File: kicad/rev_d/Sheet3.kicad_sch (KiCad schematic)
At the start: 98 parts, among them U1 74HCT1G04, X10 ST-214C, X14 AAFP/AC97 audio, X16 PLB1-4I, X17 PLB1-4I, X18 PLB1-4I, X20 PLB1-4I

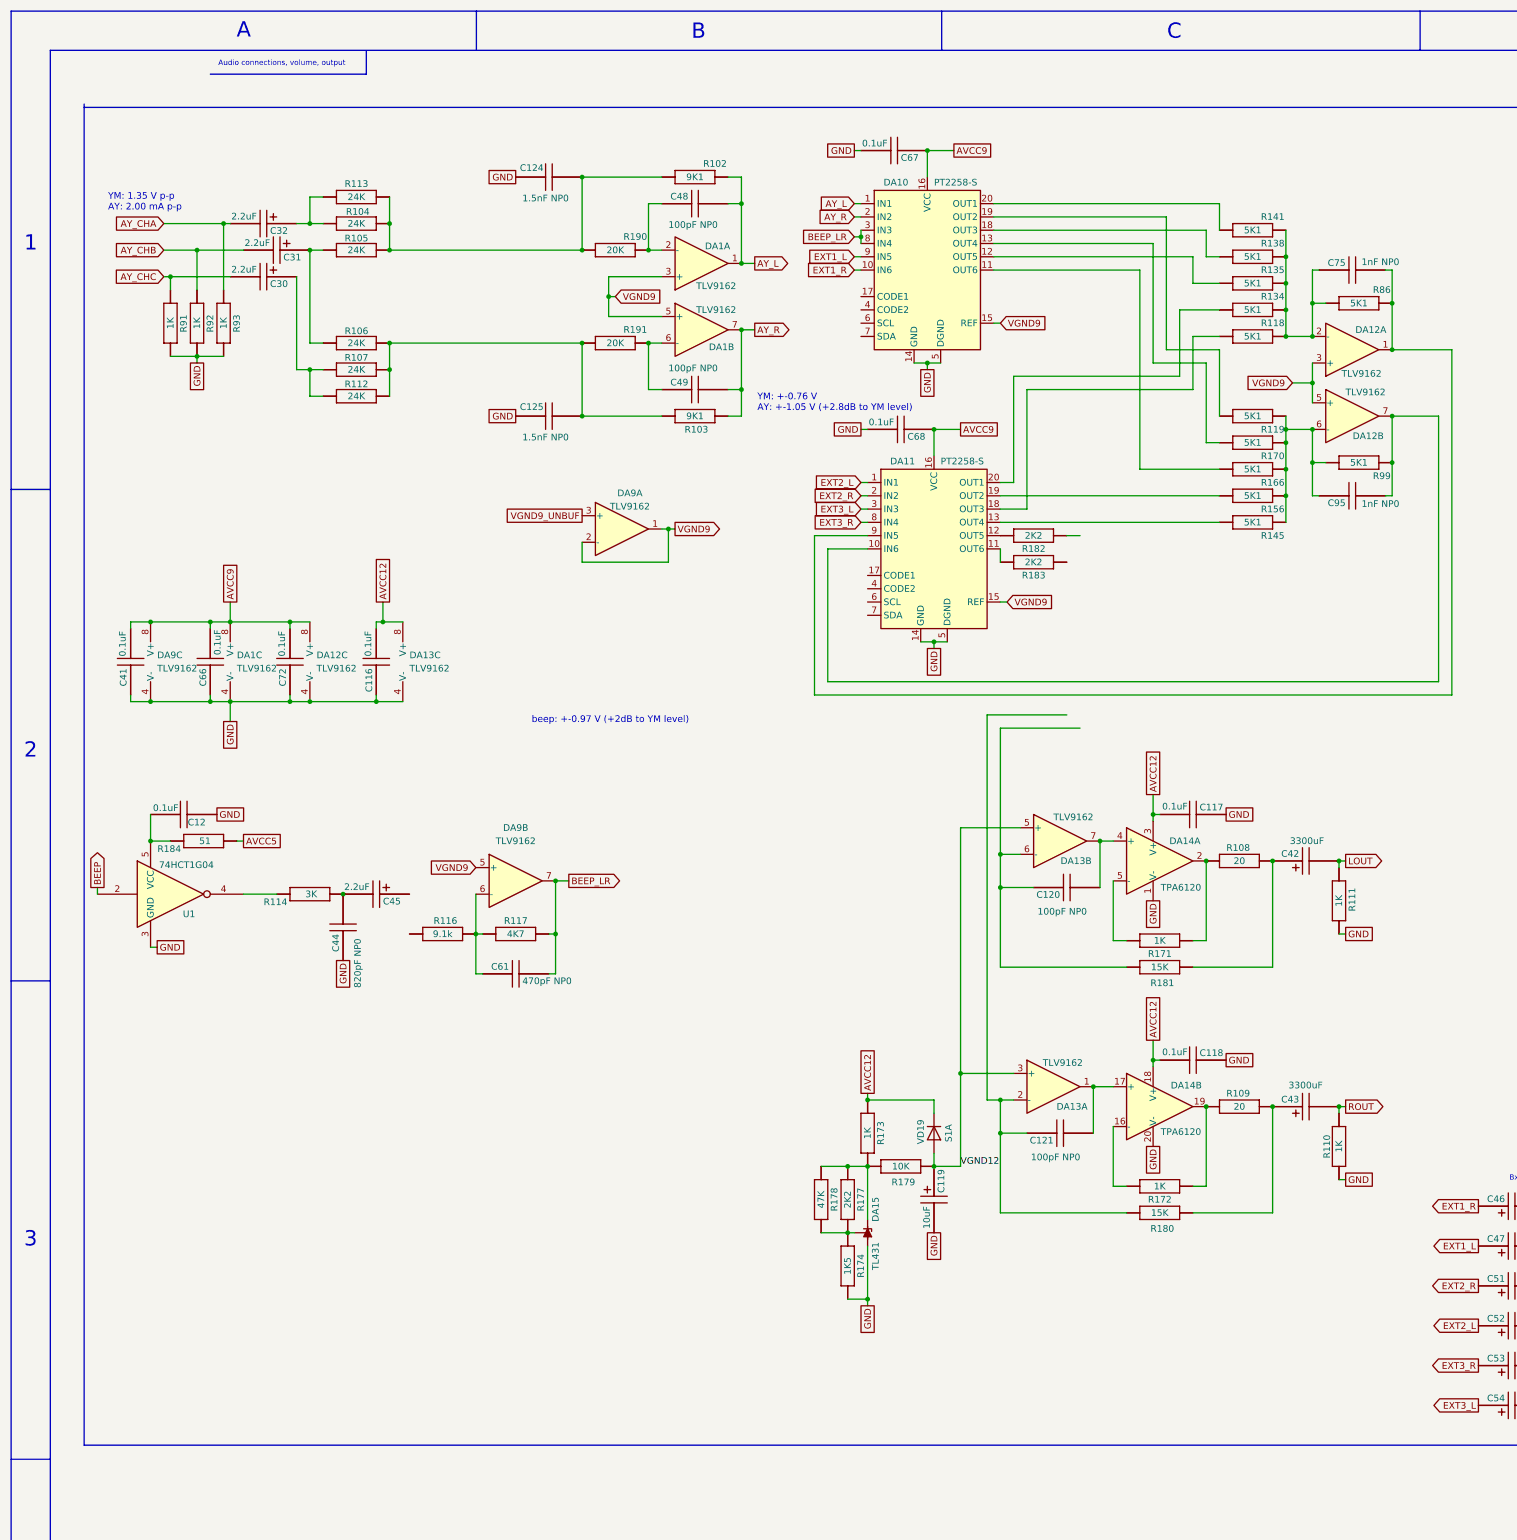
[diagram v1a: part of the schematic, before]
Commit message: pentevo: rev D: changed amplification for YM, added AY -3dB pad, remade lowpass for AY, added some ideas regarding highpass (WIP)
git-svn-id: svn://localhost/local-pentevo@1241 c6c76956-fad2-4150-a3a9-ea0a427205ba
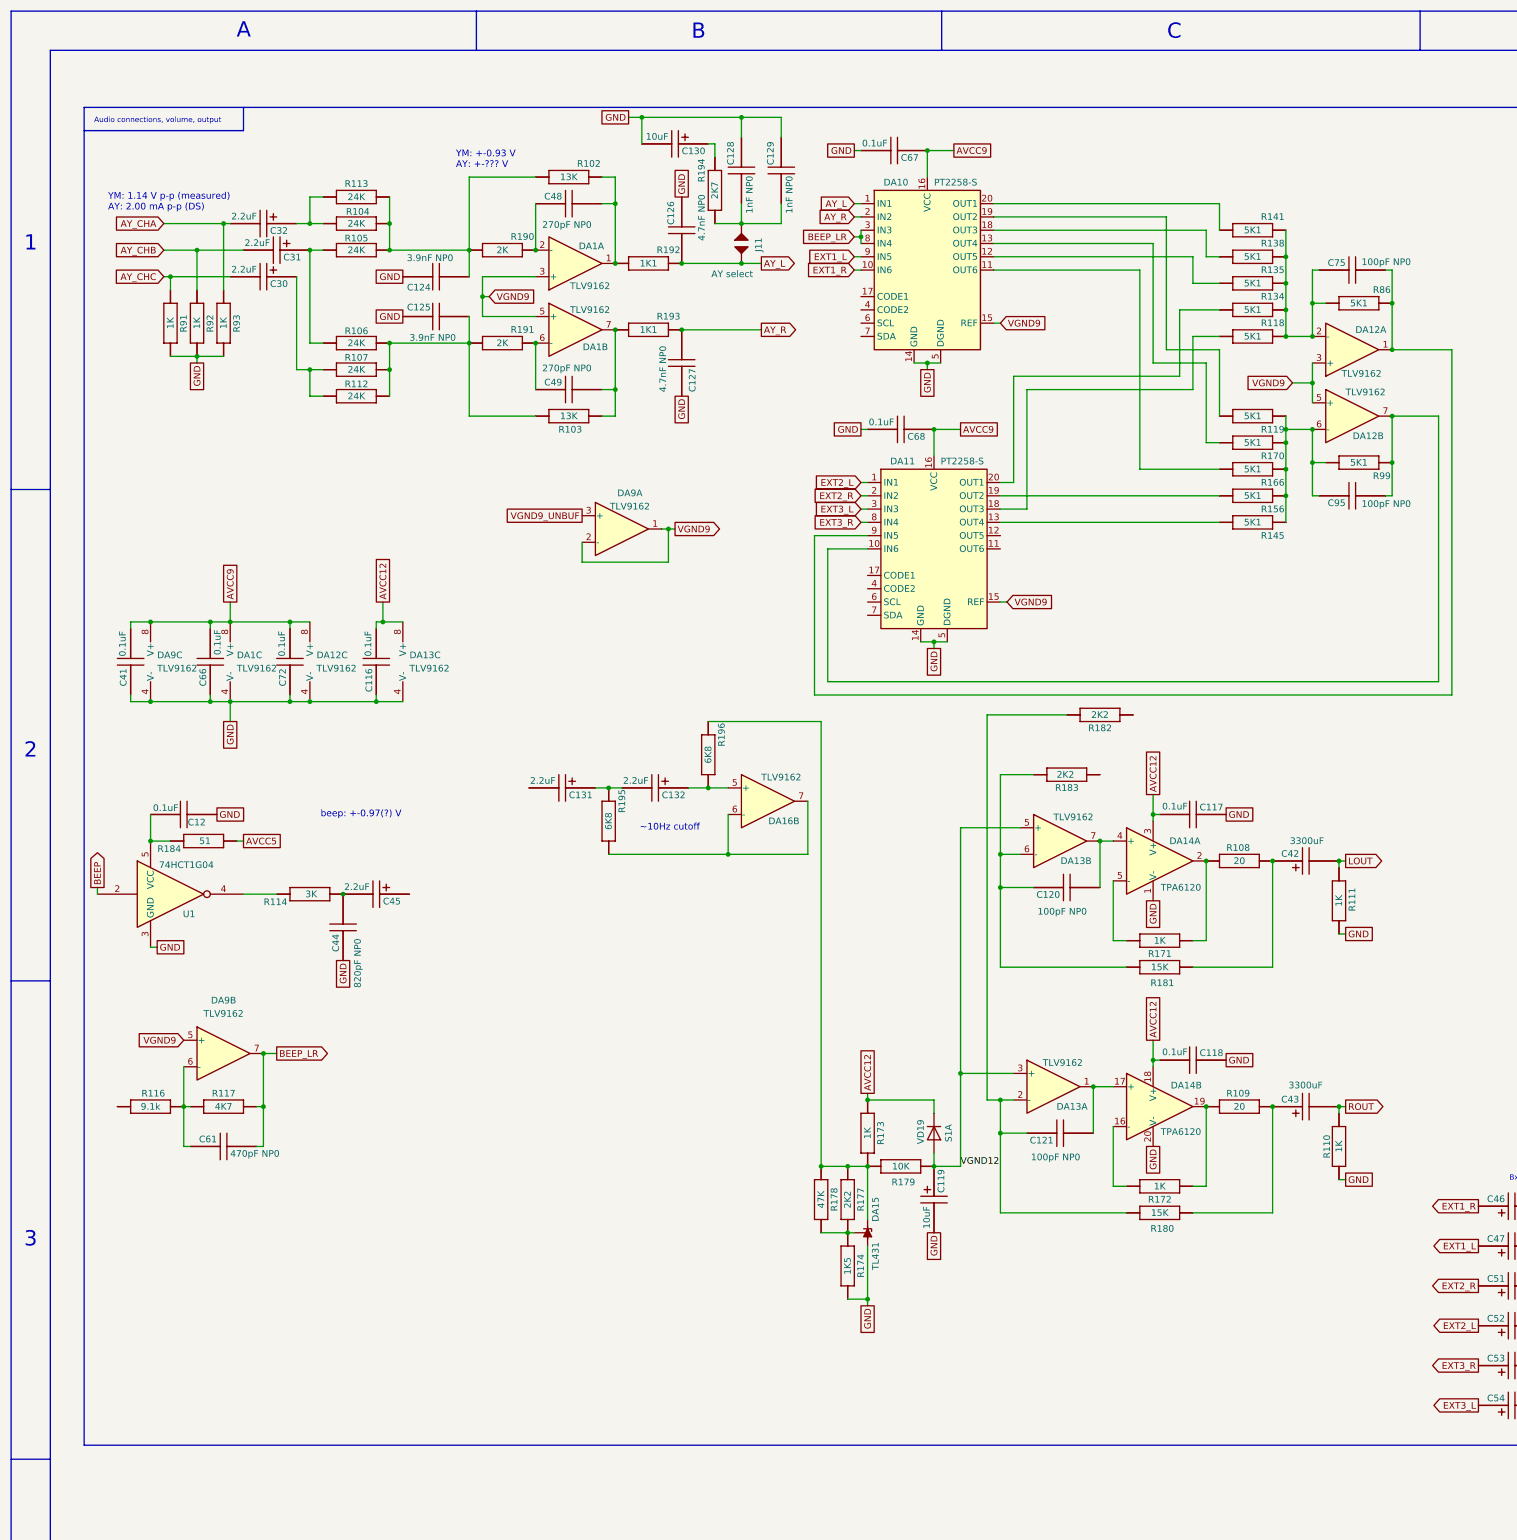
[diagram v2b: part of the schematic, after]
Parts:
- added C126, C127: 4.7nF NP0, C-CHIP, symbol eva-altium-import:Sheet2_0_CAPCHIP
- added C128, C129: 1nF NP0, C-CHIP, symbol eva-altium-import:Sheet2_0_CAPCHIP
- added C130: 10uF, EC-CHIP, symbol eva-altium-import:Sheet2_2_ECAPCHIP
- added C131, C132: 2.2uF, EC-CHIP, symbol eva-altium-import:Sheet2_2_ECAPCHIP
- added DA16: TLV9162, symbol eva-altium-import:TLC072
- added J11: JUMPER, JUMPER, symbol eva-altium-import:Sheet2_3_JUMPER
- added R192, R193: 1K1, R-CHIP, symbol eva-altium-import:Sheet2_2_mirrored_RESCHIP
- added R194: 2K7, R-CHIP, symbol eva-altium-import:Sheet2_2_mirrored_RESCHIP
- added R195, R196: 6K8, R-CHIP, symbol eva-altium-import:Sheet2_2_mirrored_RESCHIP
- C124, C125: value 1.5nF NP0 -> 3.9nF NP0
- C48, C49: value 100pF NP0 -> 270pF NP0
- C75, C95: value 1nF NP0 -> 100pF NP0
- R102, R103: value 9K1 -> 13K
- R190, R191: value 20K -> 2K
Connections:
- net AY_L: now also C126.2, J11.1 (2), R192.1 (i/o); no longer C48.2, DA1.1, R102.1 (i/o)
- net AY_R: now also C127.2, R193.1 (i/o); no longer C49.2, DA1.7, R103.1 (i/o)
- net GND: now also C126.1, C127.1, C128.1, C129.1, C130.2
- net at DA11.11 (OUT6): no longer R183.2 (i/o1)
- net at DA11.12 (OUT5): no longer R182.2 (i/o1)
- net at C121.1, DA13.2 (-), R180.1 (i/o): now also R182.2 (i/o1)
- net at DA15.1 (K), R173.2 (i/o1), R177.1 (i/o)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: now also R196.1 (i/o)
- net at C120.1, DA13.6 (-), R181.1 (i/o): now also R183.2 (i/o1)
- new net: C131.1, C132.2, R195.1 (i/o)
- new net: DA16.6 (-), DA16.7, R195.2 (i/o1)
- new net: C48.2, DA1.1, R102.1 (i/o), R192.2 (i/o1)
- new net: C49.2, DA1.7, R103.1 (i/o), R193.2 (i/o1)
- new net: C132.1, DA16.5 (+), R196.2 (i/o1)
- new net: C130.1, R194.1 (i/o)
- new net: C128.2, C129.2, J11.0 (1), R194.2 (i/o1)
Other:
- note added: "YM: +-0.93 V AY: +-??? V"
- note added: "YM: 1.14 V p-p (measured) AY: 2.00 mA p-p (DS)"
- note added: "beep: +-0.97(?) V"
- note added: "~10Hz cutoff"
- note removed: "YM: +-0.76 V AY: +-1.05 V (+2.8dB to YM level)"
- note removed: "YM: 1.35 V p-p AY: 2.00 mA p-p"
- note removed: "beep: +-0.97 V (+2dB to YM level)"
- moved on the sheet: C48, C49, C61, DA1A, DA1B, DA9B, R102, R103, R116, R117, R190, R191

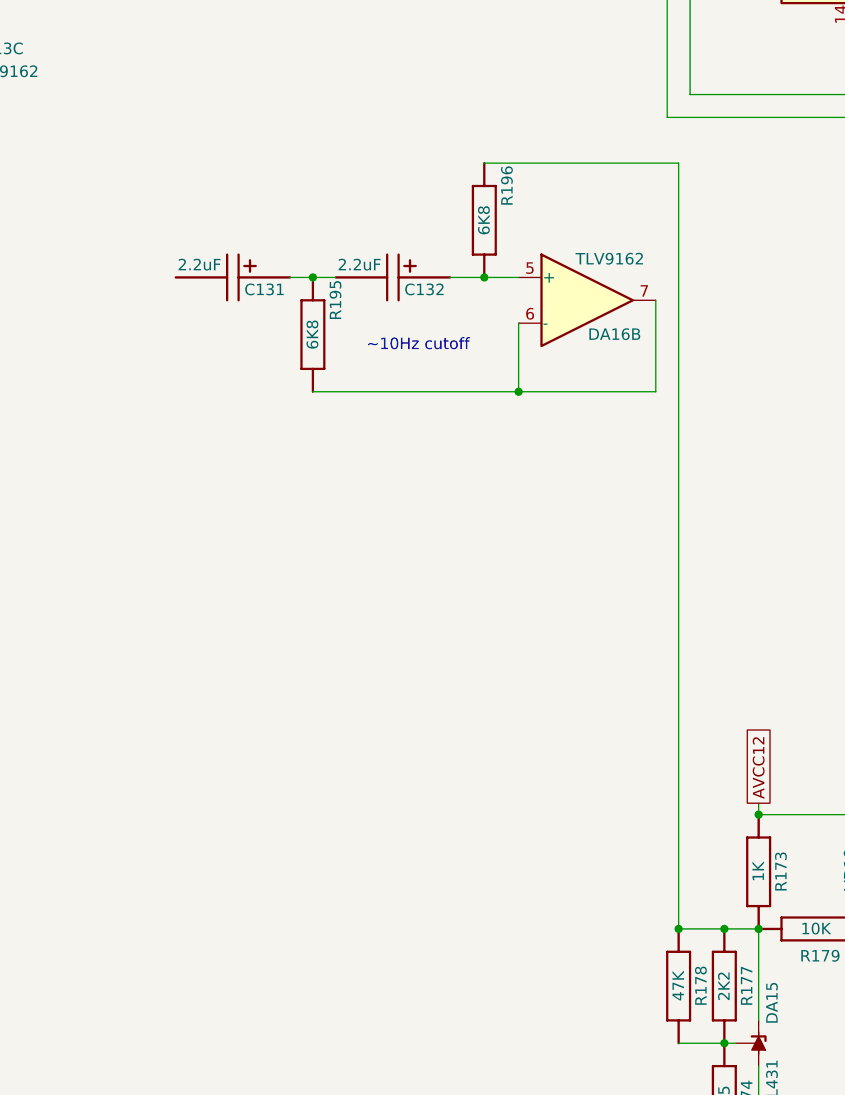
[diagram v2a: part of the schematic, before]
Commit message: pentevo: rev D: add more experimental data for YM levels, also add KC89C72 data
git-svn-id: svn://localhost/local-pentevo@1242 c6c76956-fad2-4150-a3a9-ea0a427205ba
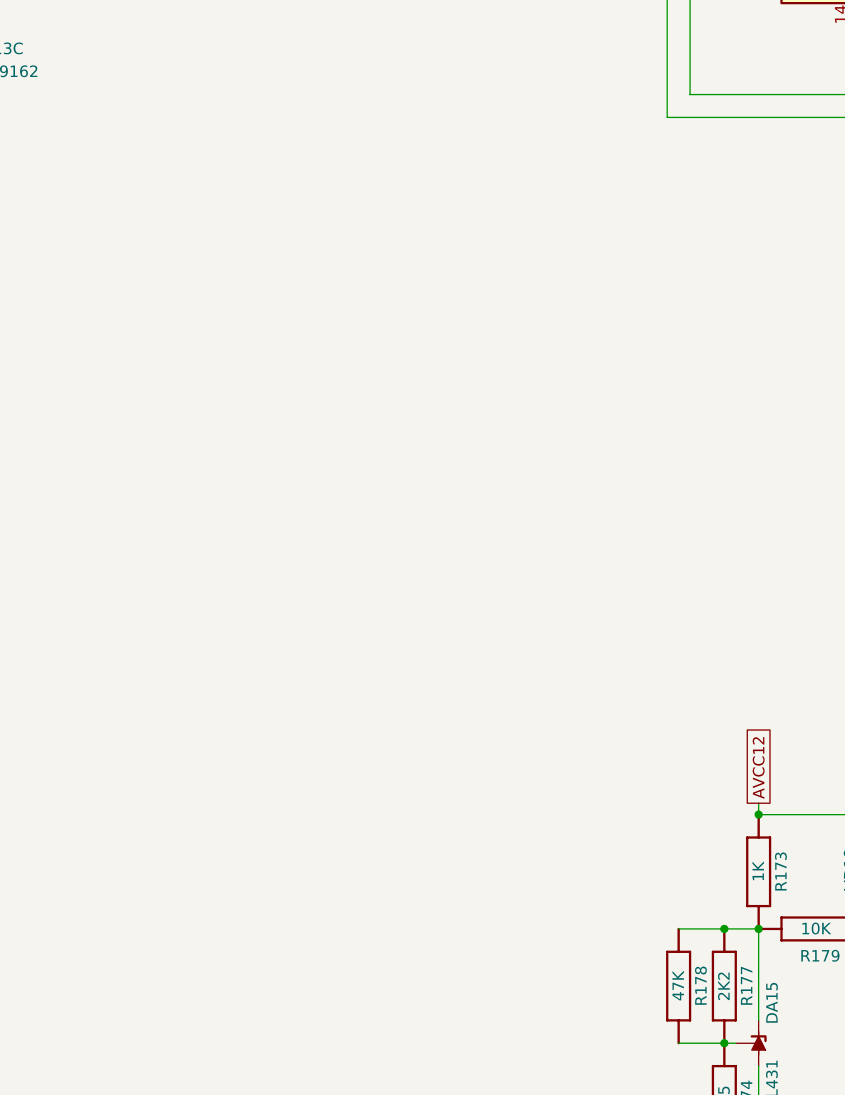
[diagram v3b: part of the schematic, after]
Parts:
- removed C131, C132: 2.2uF, EC-CHIP, symbol eva-altium-import:Sheet2_2_ECAPCHIP
- removed DA16: TLV9162, symbol eva-altium-import:TLC072
- removed R195, R196: 6K8, R-CHIP, symbol eva-altium-import:Sheet2_2_mirrored_RESCHIP
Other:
- note removed: "~10Hz cutoff"

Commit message: pentevo: rev D: finalize analog part (connect pt2258 to avr TODO)
git-svn-id: svn://localhost/local-pentevo@1256 c6c76956-fad2-4150-a3a9-ea0a427205ba
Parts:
- removed C128, C129: 1nF NP0, C-CHIP, symbol eva-altium-import:Sheet2_0_CAPCHIP
- removed C130: 10uF, EC-CHIP, symbol eva-altium-import:Sheet2_2_ECAPCHIP
- removed J11: JUMPER, JUMPER, symbol eva-altium-import:Sheet2_3_JUMPER
- removed R116: 9.1k, R-CHIP, symbol eva-altium-import:Sheet2_0_RESCHIP
- removed R194: 2K7, R-CHIP, symbol eva-altium-import:Sheet2_2_mirrored_RESCHIP
- added C128, C129: 10uF, EC-CHIP, symbol eva-altium-import:Sheet2_3_ECAPCHIP
- added C131: 6.8nF C0G, C-CHIP, symbol eva-altium-import:Sheet2_1_CAPCHIP
- added R116: 1K, R-CHIP, symbol eva-altium-import:Sheet2_2_mirrored_RESCHIP
- added R195: 6K8, R-CHIP, symbol eva-altium-import:Sheet2_2_mirrored_RESCHIP
- C120, C121: value 100pF NP0 -> 100pF C0G
- C124, C125: value 3.9nF NP0 -> 3.9nF C0G
- C126, C127: value 4.7nF NP0 -> 3.3nF C0G
- C44: value 820pF NP0 -> 1.8nF C0G
- C48, C49: value 270pF NP0 -> 270pF C0G
- C61: value 470pF NP0 -> 820pF C0G
- C75, C95: value 100pF NP0 -> 150pF C0G
- R108, R109: value 20 -> 10 1206
- R114: value 3K -> 5K1
- R184: value 51 -> 220
- R192, R193: value 1K1 -> 1K6
- X10: ALTIUM_VALUE AYout -> headphones
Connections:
- net GND: now also C131.1
- net at DA11.11 (OUT6): now also C129.2
- net at DA11.12 (OUT5): now also C128.2
- net at C61.1, DA9.6 (-): now also R116.1 (i/o); no longer R117.2 (i/o1)
- net at C45.2, R114.1 (i/o): no longer C44.2
- net at R182.1 (i/o): now also C129.1
- net at R183.1 (i/o): now also C128.1
- net at C45.1: now also C44.2, R195.2 (i/o1)
- new net: C131.2, R116.2 (i/o1), R117.2 (i/o1), R195.1 (i/o)
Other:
- note added: "beep: +-0.99 V"
- note removed: "beep: +-0.97(?) V"
- moved on the sheet: C116, C119, C12, C41, C44, C45, C46, C47, C51, C52, C53, C54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
